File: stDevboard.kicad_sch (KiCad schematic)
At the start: 20 parts, among them IC1 NCP189CMTW330TAG, J1 USB_C_Receptacle_USB2.0_14P, U1 STM32U585CIUxQ

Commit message: worked on schematic
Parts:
- added BOOT1: SW_SPDT, symbol Switch:SW_SPDT
- added C14: 100 nF, symbol Device:C
- added D1: D_Zener, symbol Device:D_Zener
- added R4: 10k, symbol Device:R
- added RESET1: SW_Push, symbol Switch:SW_Push
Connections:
- net +3.3V: now also BOOT1.3 (C)
- net GND: now also U1.24 (VSS), U1.35 (VSS), U1.47 (VSS), U1.49 (VSS), U1.8 (VSSA), BOOT1.1 (A), C14.1, D1.2 (A), RESET1.1
- net at U1.44 (PH3): now also R4.2
- net at U1.7 (NRST): now also C14.2, D1.1 (K), RESET1.2
- new net: BOOT1.2 (B), R4.1

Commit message: worked some more on schematic, also figured out more of oscillator stuff and boot button
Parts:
- added C15: C, symbol Device:C
- added Y1: 32.768 kHz, Crystal:Crystal_SMD_MicroCrystal_CC8V-T1A-2Pin_2.0x1.2mm, symbol Device:Crystal
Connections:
- net at U1.5 (PH0): now also Y1.1
- net at U1.6 (PH1): now also Y1.2
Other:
- note added: "for boot - pull down to ground for normal operation, pull high for dfu mode"
- moved on the sheet: BOOT1

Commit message: worked on a ton of stuff, see journal for details
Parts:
- removed BOOT1: SW_SPDT, symbol Switch:SW_SPDT
- removed Y1: 32.768 kHz, Crystal:Crystal_SMD_MicroCrystal_CC8V-T1A-2Pin_2.0x1.2mm, symbol Device:Crystal
- added BOOT1: SW_Push, symbol Switch:SW_Push
- added C16, C18, C20: 2.2uF, symbol Device:C
- added C17, C21: 0.1uF, symbol Device:C
- added C19, C22: 10nF, symbol Device:C
- added IC2: MMC5603NJ, MMC5603NJ, symbol MMC5603NJ:MMC5603NJ
- added IC3: ICM-42670-P, ICM42670P, symbol ICM-42670-P:ICM-42670-P
- added IC4: ICM-45686, ICM42670P, symbol ICM-42670-P:ICM-42670-P
- added R5: 100k, symbol Device:R
- added R6, R7, R8, R9: 2.7k, symbol Device:R
- added U2: BMP581, BMP581, symbol BMP581:BMP581
- C15: value C -> 100 nF
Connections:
- net +3.3V: now also C15.2, BOOT1.1, C16.2, C17.1, C18.1, C19.1, C20.1, C21.1, C22.1, IC2.B1 (VDD), IC3.1 (AP_SDO_/_AP_AD0), IC3.12 (AP_CS), IC3.5 (VDDIO), IC3.8 (VDD), IC4.1 (AP_SDO_/_AP_AD0), IC4.12 (AP_CS), IC4.5 (VDDIO), IC4.8 (VDD), R8.2, R9.2, U2.1 (VDDIO), U2.10 (VDD), U2.6 (CSB)
- net GND: now also C15.1, C16.1, C17.2, C18.2, C19.2, C20.2, C21.2, C22.2, IC2.A1 (VSA), IC3.6 (GND), IC3.7 (FSYNC), IC4.6 (GND), IC4.7 (FSYNC), R5.2, U2.3 (VSS_1), U2.5 (SDO), U2.8 (VSS_2), U2.9 (VSS_3)
- net at R4.1: now also BOOT1.2, R5.1
- net i2c1_sda: now reaches U1.43 (PB7)
- net i2c1_sda: now also IC3.14 (AP_SDA_/_AP_SDIO_/_AP_SDI), IC4.14 (AP_SDA_/_AP_SDIO_/_AP_SDI), R7.2, R8.1, U2.4 (SDI)
- net i2c1_sck: now reaches U1.45 (PB8)
- net i2c1_sck: now also IC3.13 (AP_SCL_/_AP_SCLK), IC4.13 (AP_SCL_/_AP_SCLK), R6.2, R9.1, U2.2 (SCK)
- new net: IC2.A2 (SCL), R6.1
- new net: IC2.B2 (SDA), R7.1
- new net bmp_int: U2.7 (INT)
- new net highrate_highg_int1: IC4.4 (INT1_/_INT)
- new net highrate_highg_int2: IC4.9 (INT2)
- new net lowrate_lowg_int1: IC3.4 (INT1_/_INT)
- new net lowrate_lowg_int2: IC3.9 (INT2)
- no-connect marks 0 -> 8
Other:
- added sheet mosfets (mosfets.kicad_sch)
- note added: "absolute mess of decoupling capacitors"
- note removed: "for boot - pull down to ground for normal operation, pull high for dfu mode"
- moved on the sheet: J1, L1, R2, R3

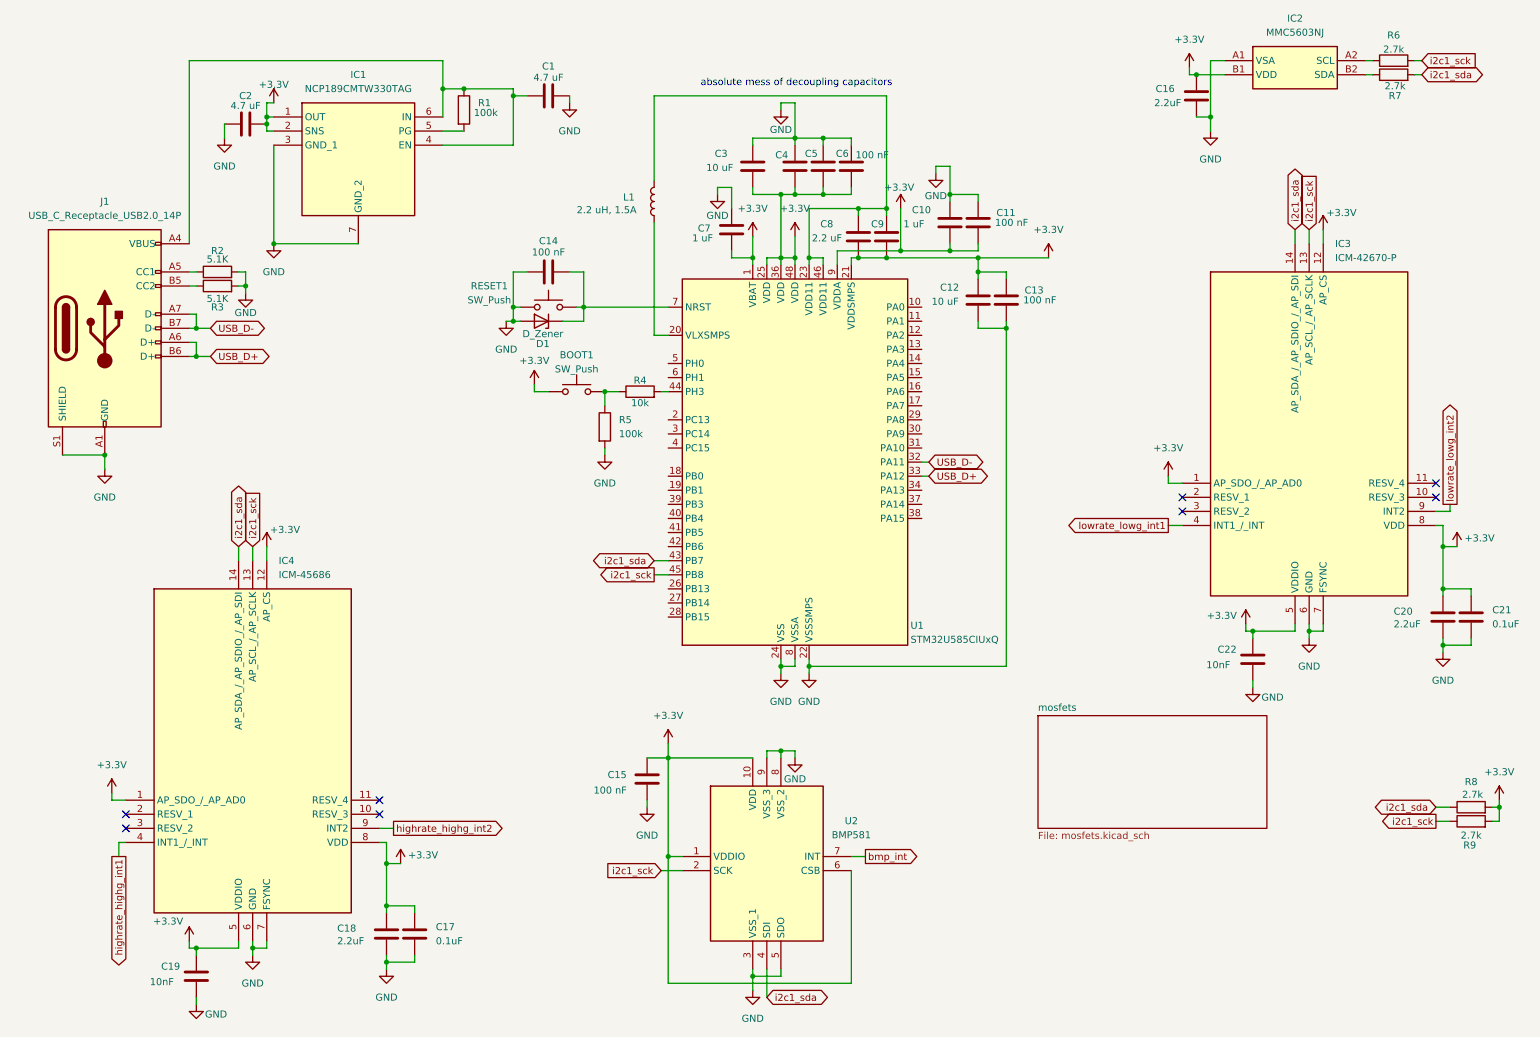
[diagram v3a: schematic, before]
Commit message: everything I did while on vacation - initial schematic finished, footprints mostly assigned, and pcb layout started
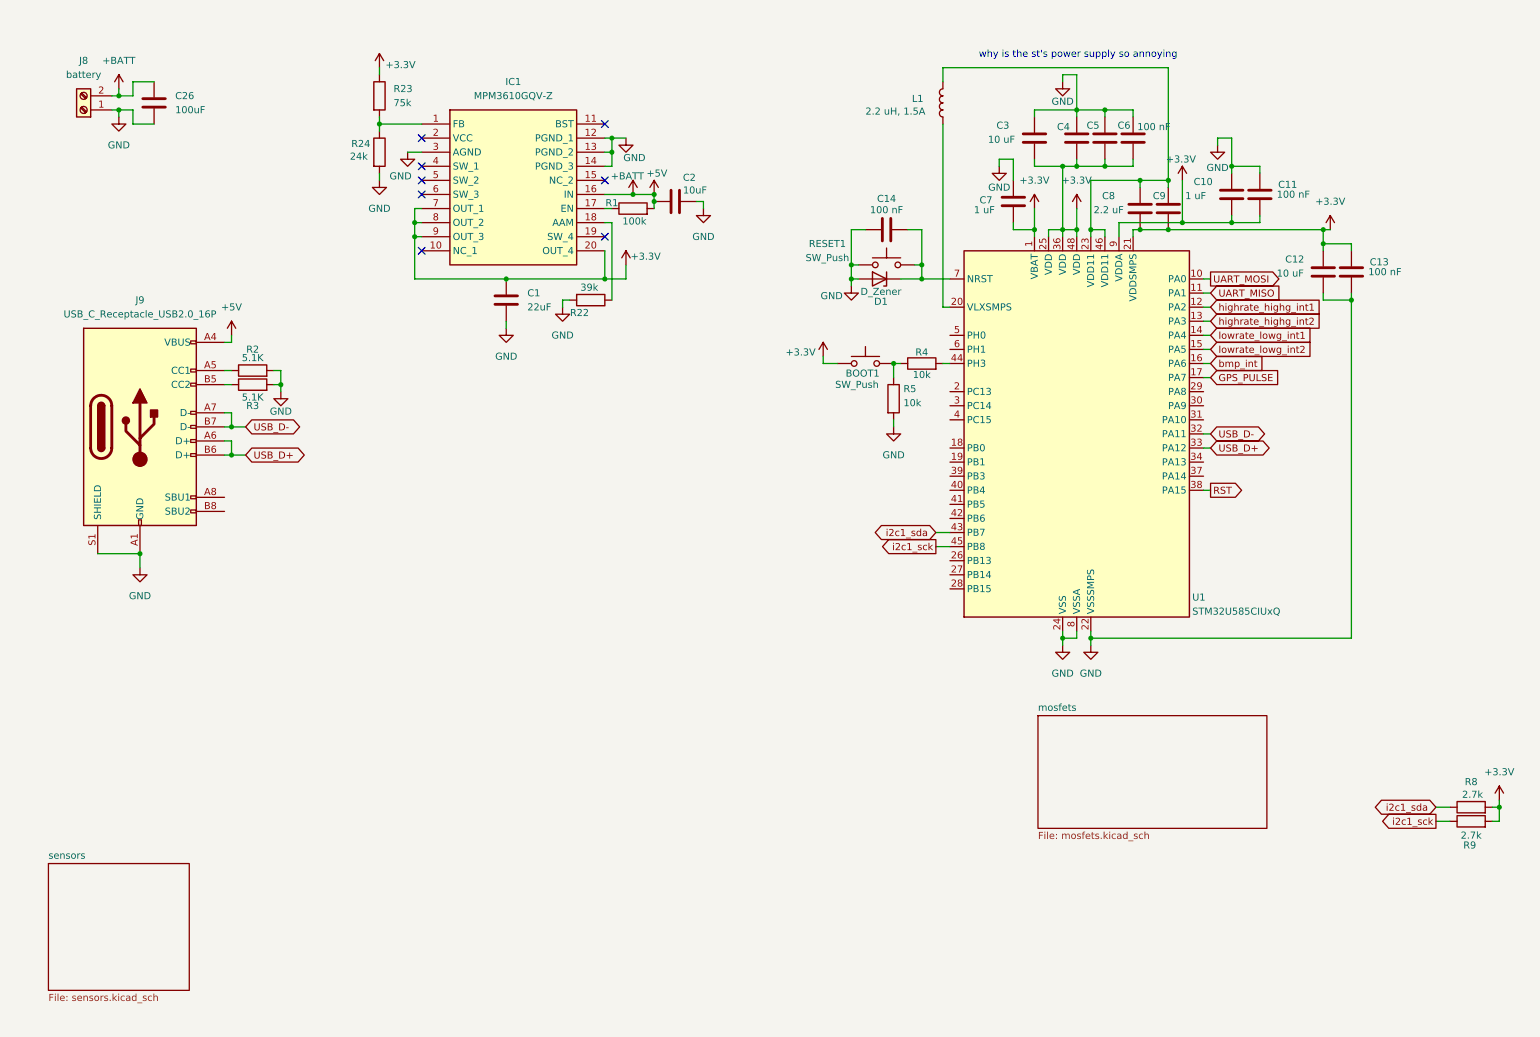
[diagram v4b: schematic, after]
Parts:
- removed C15: 100 nF, symbol Device:C
- removed C16, C18, C20: 2.2uF, symbol Device:C
- removed C17, C21: 0.1uF, symbol Device:C
- removed C19, C22: 10nF, symbol Device:C
- removed IC1: NCP189CMTW330TAG, SON65P200X200X80-7N, symbol NCP189CMTW330TAG:NCP189CMTW330TAG
- removed IC2: MMC5603NJ, MMC5603NJ, symbol MMC5603NJ:MMC5603NJ
- removed IC3: ICM-42670-P, ICM42670P, symbol ICM-42670-P:ICM-42670-P
- removed IC4: ICM-45686, ICM42670P, symbol ICM-42670-P:ICM-42670-P
- removed J1: USB_C_Receptacle_USB2.0_14P, symbol Connector:USB_C_Receptacle_USB2.0_14P
- removed R6, R7: 2.7k, symbol Device:R
- removed U2: BMP581, BMP581, symbol BMP581:BMP581
- added C26: 100uF, Capacitor_SMD:C_0805_2012Metric, symbol Device:C
- added IC1: MPM3610GQV-Z, footprints:MPM3606GQVZ, symbol MPM3610GQV-Z:MPM3610GQV-Z
- added J8: battery, symbol Connector:Screw_Terminal_01x02
- added J9: USB_C_Receptacle_USB2.0_16P, Connector_USB:USB_C_Receptacle_GCT_USB4085, symbol Connector:USB_C_Receptacle_USB2.0_16P
- added R22: 39k, Resistor_SMD:R_0201_0603Metric, symbol Device:R
- added R23: 75k, Resistor_SMD:R_0201_0603Metric, symbol Device:R
- added R24: 24k, Resistor_SMD:R_0201_0603Metric, symbol Device:R
- C1: value 4.7 uF -> 22uF; footprint (none) -> Capacitor_SMD:C_0603_1608Metric
- C10, C12, C3, C7, C8, C9: footprint (none) -> Capacitor_SMD:C_0603_1608Metric
- C11, C13, C14, C4, C5, C6: footprint (none) -> Capacitor_SMD:C_0402_1005Metric
- C2: value 4.7 uF -> 10uF; footprint (none) -> Capacitor_SMD:C_0603_1608Metric
- D1: footprint (none) -> Diode_SMD:D_0402_1005Metric
- L1: footprint (none) -> footprints:INDC2520X120N
- R1, R2, R3, R4, R8, R9: footprint (none) -> Resistor_SMD:R_0402_1005Metric
- R5: value 100k -> 10k; footprint (none) -> Resistor_SMD:R_0402_1005Metric
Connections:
- net +3.3V: now also C1.2, IC1.20 (OUT_4), IC1.7 (OUT_1), IC1.8 (OUT_2), IC1.9 (OUT_3), R23.1; no longer C2.2
- net GND: now also C1.1, C2.2, C26.2, IC1.12 (PGND_1), IC1.13 (PGND_2), IC1.14 (PGND_3), IC1.3 (AGND), J8.1 (Pin_1), J9.A1 (GND), J9.A12 (GND), J9.B1 (GND), J9.B12 (GND), J9.S1 (SHIELD), R22.2, R24.2; no longer C1.2, C2.1
- net USB_D+: now also J9.A6 (D+), J9.B6 (D+)
- net USB_D-: now also J9.A7 (D-), J9.B7 (D-)
- net bmp_int: now also U1.16 (PA6)
- net highrate_highg_int1: now also U1.12 (PA2)
- net highrate_highg_int2: now also U1.13 (PA3)
- net lowrate_lowg_int1: now also U1.14 (PA4)
- net lowrate_lowg_int2: now also U1.15 (PA5)
- net at R2.1: now also J9.A5 (CC1)
- net at R1.1: now also IC1.17 (EN); no longer C1.1
- net +5V: now reaches R1.2
- net +5V: now also C2.1, C26.1, IC1.16 (IN), J8.2 (Pin_2), J9.A4 (VBUS), J9.A9 (VBUS), J9.B4 (VBUS), J9.B9 (VBUS)
- net at R3.1: now also J9.B5 (CC2)
- net UART_MOSI: now reaches U1.10 (PA0)
- net UART_MISO: now reaches U1.11 (PA1)
- net GPS_PULSE: now reaches U1.17 (PA7)
- net RST: now reaches U1.38 (PA15)
- new net: IC1.1 (FB), R23.2, R24.1
- new net: IC1.18 (AAM), R22.1
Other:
- added sheet sensors (sensors.kicad_sch)
- note added: "why is the st's power supply so annoying"
- note removed: "absolute mess of decoupling capacitors"
- moved on the sheet: BOOT1, C10, C11, C12, C13, C14, C3, C4, C5, C6, C7, C8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

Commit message: pcb coming along, schematic way more done - I now have a lot more respect for hardware people than I did earlier
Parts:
- J8: footprint (none) -> Connector_PinHeader_2.54mm:PinHeader_1x02_P2.54mm_Vertical
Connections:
- net c1_test: now reaches U1.18 (PB0)
- net c2_test: now reaches U1.19 (PB1)
- net cont_test: now reaches U1.37 (PA14)
- net c3_test: now reaches U1.39 (PB3)
- net c4_test: now reaches U1.40 (PB4)
- net c5_test: now reaches U1.41 (PB5)
- net c6_test: now reaches U1.42 (PB6)
- no-connect marks 8 -> 22
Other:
- moved on the sheet: R5

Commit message: tons of work, see journal for details
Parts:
- removed BOOT1, RESET1: SW_Push, symbol Switch:SW_Push
- removed C14: 100 nF, Capacitor_SMD:C_0402_1005Metric, symbol Device:C
- removed D1: D_Zener, Diode_SMD:D_0402_1005Metric, symbol Device:D_Zener
- added BOOT, RST1: Conn_01x02, symbol Connector_Generic:Conn_01x02
- added J7: UART, symbol Connector_Generic:Conn_01x03
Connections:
- net c6_test is gone; now on net i2c1_sck: U1.42 (PB6)
- net +3.3V: now also BOOT.1 (Pin_1)
- net GND: now also R5.1, J7.3 (Pin_3), RST1.1 (Pin_1); no longer R5.2
- net bmp_int: now also U1.45 (PB8); no longer U1.16 (PA6)
- net i2c1_sck: no longer U1.45 (PB8)
- net at U1.7 (NRST): now also RST1.2 (Pin_2)
- net at R4.1: now also R5.2, BOOT.2 (Pin_2); no longer R5.1
- net gps_int: now reaches U1.29 (PA8)
- net at U1.30 (PA9): now also J7.1 (Pin_1)
- net at U1.31 (PA10): now also J7.2 (Pin_2)
- net GPS_PULSE renamed spi_mosi
- net RST: no longer names the net of U1.38 (PA15)
- net UART_MISO renamed telem_rst
- net UART_MOSI renamed gps_rst
- net c1_test renamed imu1_int1
- net c2_test renamed imu1_int2
- net c3_test renamed imu2_int1
- net c4_test renamed imu2_int2
- net c5_test renamed mag_int
- net cont_test: no longer names the net of U1.37 (PA14)
- net highrate_highg_int1 renamed mos_rst
- net highrate_highg_int2 renamed gps_pulse
- net lowrate_lowg_int1 renamed spi_nss
- net lowrate_lowg_int2 renamed spi_sclk
- new net spi_miso: U1.16 (PA6)
- no-connect marks 22 -> 10
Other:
- added sheet rf (rf.kicad_sch)
- note added: "todo: actually use oscillators (apparantly you need them for usb stability) also check which pins are jtab/swd"
- moved on the sheet: R5

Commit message: oops forgot to commit - looks like I worked on the lr2021's symbol and the schematic - see journal for details on what I did
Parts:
- added R16: 10k, symbol Device:R
- added U4: STM32U073KCUx, Package_DFN_QFN:QFN-32-1EP_5x5mm_P0.5mm_EP3.45x3.45mm, symbol MCU_ST_STM32U0:STM32U073KCUx
- added Y2: ECS-160-8-36B2-CKM-TR, ECS160836B2CKMTR, symbol ECS-160-8-36B2-CKM-TR:ECS-160-8-36B2-CKM-TR
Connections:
- net +3.3V: now also R16.2
- net at RST1.2 (Pin_2), U1.7 (NRST): now also R16.1
- new net: U4.16 (VSS), U4.32 (VSS), U4.33 (VSS)
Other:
- note added: "todo: actually use oscillators (apparantly you need them for usb stability) also check which pins are jtab/swd also check to see if we need pullups/pulldowns on boot/rst"
- note removed: "todo: actually use oscillators (apparantly you need them for usb stability) also check which pins are jtab/swd"
- moved on the sheet: RST1

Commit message: tons of progress on schematic and pcb - see journal for details
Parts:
- removed BOOT, RST1: Conn_01x02, symbol Connector_Generic:Conn_01x02
- removed C10, C7: 1 uF, Capacitor_SMD:C_0603_1608Metric, symbol Device:C
- removed C11, C13, C4, C5, C6: 100 nF, Capacitor_SMD:C_0402_1005Metric, symbol Device:C
- removed C12, C3: 10 uF, Capacitor_SMD:C_0603_1608Metric, symbol Device:C
- removed C8, C9: 2.2 uF, Capacitor_SMD:C_0603_1608Metric, symbol Device:C
- removed J7: UART, symbol Connector_Generic:Conn_01x03
- removed L1: 2.2 uH, 1.5A, footprints:INDC2520X120N, symbol Device:L
- removed R16: 10k, symbol Device:R
- removed R4, R5: 10k, Resistor_SMD:R_0402_1005Metric, symbol Device:R
- removed U1: STM32U585CIUxQ, Package_DFN_QFN:QFN-48-1EP_7x7mm_P0.5mm_EP5.6x5.6mm, symbol MCU_ST_STM32U5:STM32U585CIUxQ
- removed U4: STM32U073KCUx, Package_DFN_QFN:QFN-32-1EP_5x5mm_P0.5mm_EP3.45x3.45mm, symbol MCU_ST_STM32U0:STM32U073KCUx
- removed Y2: ECS-160-8-36B2-CKM-TR, ECS160836B2CKMTR, symbol ECS-160-8-36B2-CKM-TR:ECS-160-8-36B2-CKM-TR
- added D4: D_Schottky, Diode_SMD:D_0805_2012Metric, symbol Device:D_Schottky
- added FB1, FB2: BLM15AX102SN1D, footprints:NFZ15SG152SN10B, symbol Device:FerriteBead
- added J11: USB_C_Receptacle_USB2.0_16P, Connector_USB:USB_C_Receptacle_GCT_USB4085, symbol Connector:USB_C_Receptacle_USB2.0_16P
- added J3: Conn_02x03_Top_Bottom, Connector_PinHeader_2.54mm:PinHeader_2x02_P2.54mm_Vertical, symbol Connector_Generic:Conn_02x03_Top_Bottom
- added R23, R24: 5.1K, Resistor_SMD:R_0402_1005Metric, symbol Device:R
- C1: renamed from C26; value 100uF -> 10uF
- renumbered C1 to C2, C2 to C3, J8 to J1, J9 to J2, R2 to R1, R8 to R12, R9 to R13, R3 to R2, R23 to R3, R24 to R4, R22 to R5, R1 to R6
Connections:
- net +3.3V: now also J3.6 (Pin_6)
- net +5V: now also D4.2 (A), J11.A4 (VBUS), J11.A9 (VBUS), J11.B4 (VBUS), J11.B9 (VBUS); no longer C1.1, C3.1, IC1.16 (IN), J1.2 (Pin_2), R6.2
- net GND: now also FB1.2, FB2.2, J11.A1 (GND), J11.A12 (GND), J11.B1 (GND), J11.B12 (GND), J3.3 (Pin_3), R23.2, R24.2; no longer J2.S1 (SHIELD)
- new net: J11.B5 (CC2), R24.1
- new net: FB1.1, J2.S1 (SHIELD)
- new net: J11.A5 (CC1), R23.1
- new net: FB2.1, J11.S1 (SHIELD)
- new net +BATT: C1.1, C3.1, D4.1 (K), IC1.16 (IN), J1.2 (Pin_2), R6.2
- new net USB2_D+: J11.A6 (D+), J11.B6 (D+)
- new net USB2_D-: J11.A7 (D-), J11.B7 (D-)
- new net mpu_rx_external: J3.2 (Pin_2)
- new net mpu_tx_external: J3.1 (Pin_1)
- new net ppu_rx_external: J3.5 (Pin_5)
- new net ppu_tx_external: J3.4 (Pin_4)
- no-connect marks 10 -> 12
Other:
- added sheet main micro (mpu.kicad_sch)
- added sheet peripheral micro (ppu.kicad_sch)
- note removed: "todo: actually use oscillators (apparantly you need them for usb stability) also check which pins are jtab/swd also check to see if we need pullups/pulldowns on boot/rst"
- note removed: "why is the st's power supply so annoying"
- moved on the sheet: C1, C2, C3, IC1, J1, J2, R1, R2, R3, R4, R5, R6
